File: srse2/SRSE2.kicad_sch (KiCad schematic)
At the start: 83 parts, among them J1 s88-N, J2 CAN, J3 RJ45_Hanrun_HR911105A_Horizon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, P1 I2S, P10 PIC_SPARE, P11 RS485 TERM, P12 RS485, P13 CONN_01X03, P15 RA5, P17 RA5, P18 CONN_01X03, P19 CONN_01X02, P2 CONN_01X09, P20 O2P-Rst, P3 CONN_01X02, P4 CONN_01X04, P5 CONN_01X04, P6 ISO_I2C, P7 CAN_TERM, P8 CAN, P9 PIC_I2C, U1 Omega2, U2 ADuM1250, U3 SN65HVD230, U4 PIC18F25K80, U6 MAX485, U7 TPS5430DDA, U8 CD4504, U9 LM317, Y1 16MHz

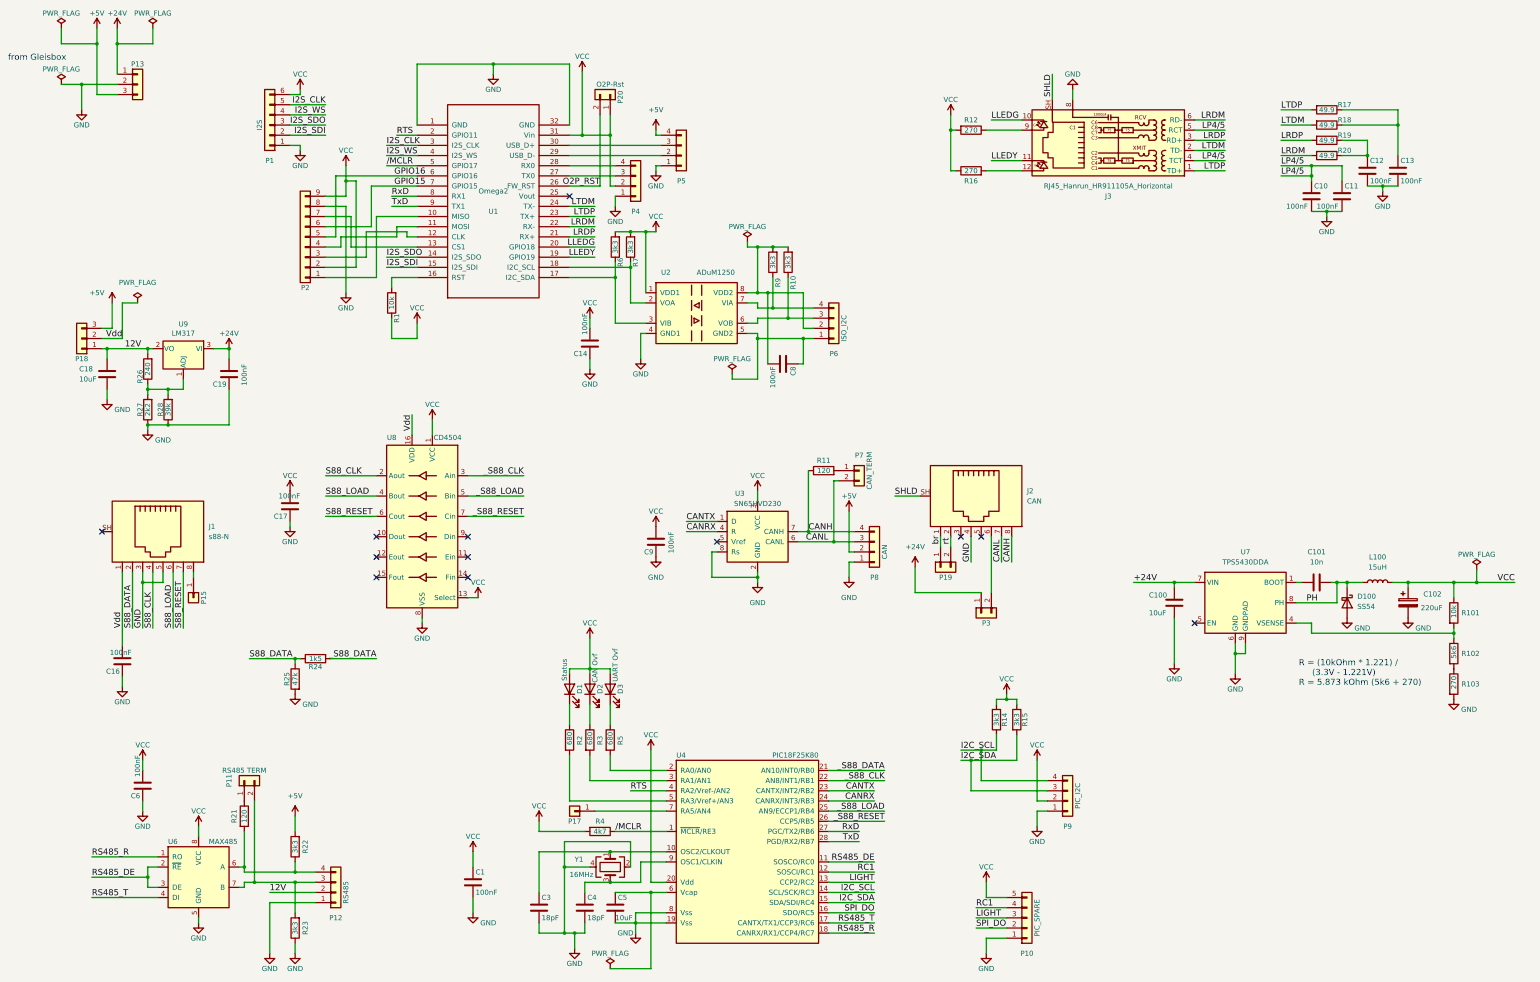
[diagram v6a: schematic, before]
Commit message: update to KiCad 7.0 - wip
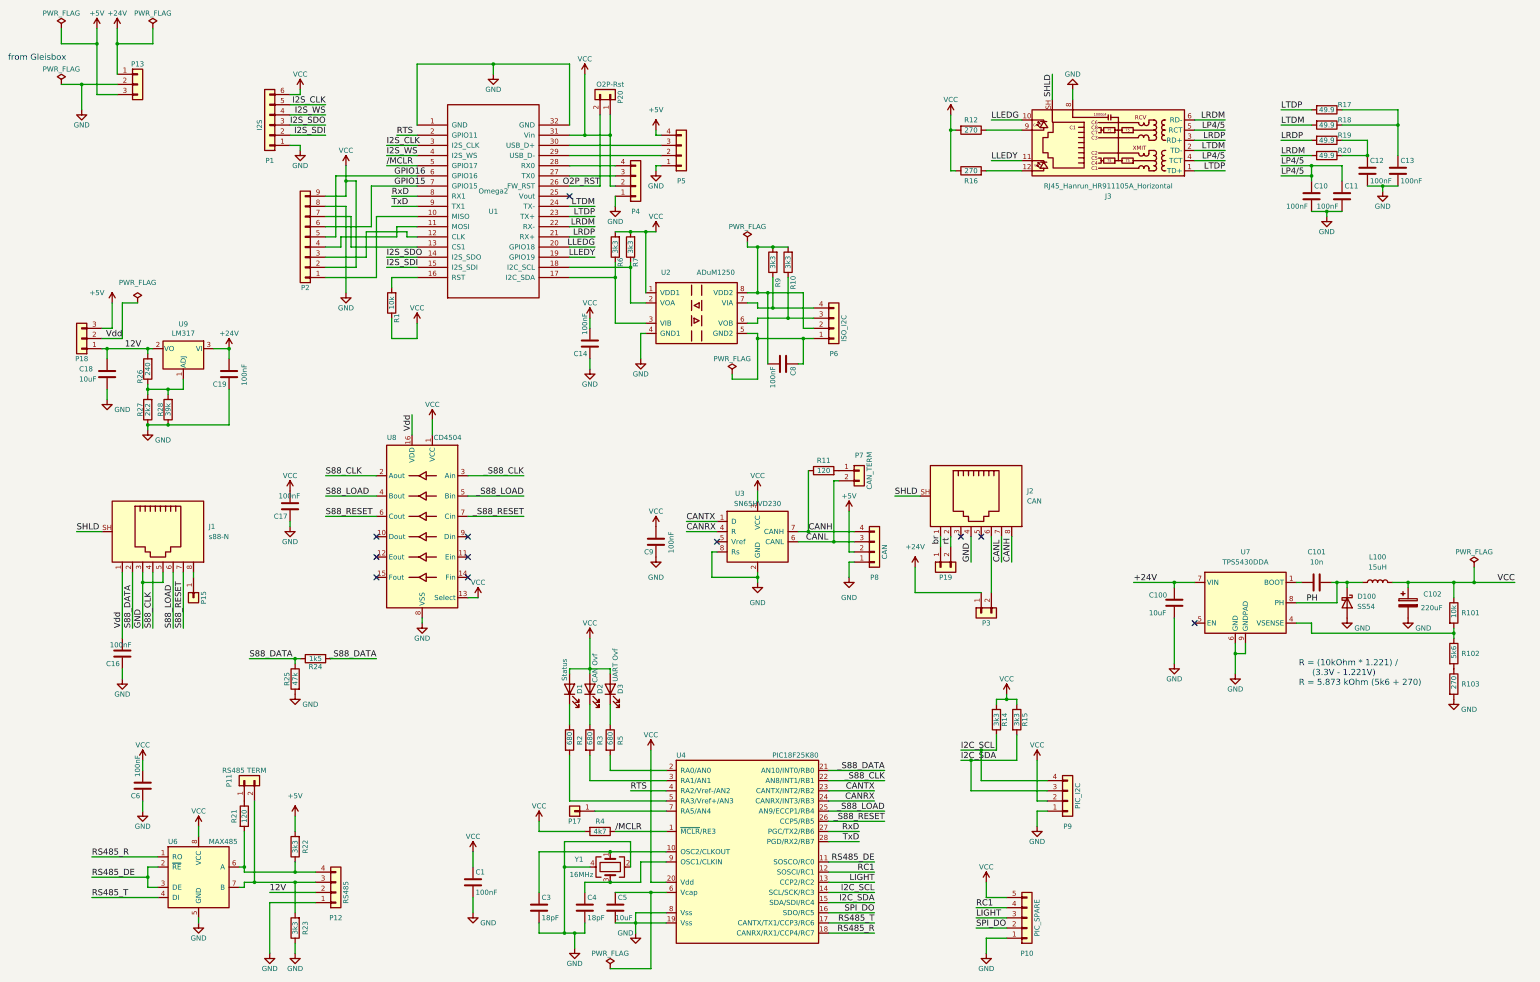
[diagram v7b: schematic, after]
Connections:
- net SHLD: now also J1.SH
- no-connect marks 12 -> 11
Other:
- moved on the sheet: C16
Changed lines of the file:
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@@
   (junction (at 175.26 86.36) (diameter 0) (color 0 0 0 0)
   )
-  (junction (at 386.715 173.99) (diameter 0) (color 0 0 0 0)
-  )
   (junction (at 175.26 95.25) (diameter 0) (color 0 0 0 0)
   )
@@
   (junction (at 354.33 173.99) (diameter 0) (color 0 0 0 0)
   )
+  (junction (at 386.08 173.99) (diameter 0) (color 0 0 0 0)
+  )
   (junction (at 158.75 261.62) (diameter 0) (color 0 0 0 0)
   )
@@
   (junction (at 207.01 113.03) (diameter 0) (color 0 0 0 0)
   )
-  (junction (at 163.195 62.23) (diameter 0) (color 0 0 0 0)
+  (junction (at 163.83 62.23) (diameter 0) (color 0 0 0 0)
   )
   (junction (at 367.03 59.69) (diameter 0) (color 0 0 0 0)
@@
   (no_connect (at 196.85 163.83))
   (no_connect (at 262.89 162.56))
-  (no_connect (at 43.18 161.29))
   (no_connect (at 111.76 167.64))
   (no_connect (at 111.76 162.56))
@@
     (stroke (width 0) (type default))
   )
+  (wire (pts (xy 163.83 62.23) (xy 170.18 62.23))
+    (stroke (width 0) (type default))
+  )
   (wire (pts (xy 74.93 125.73) (xy 74.93 134.62))
     (stroke (width 0) (type default))
@@
     (stroke (width 0) (type default))
   )
-  (wire (pts (xy 386.715 170.815) (xy 386.715 173.99))
+  (wire (pts (xy 386.08 170.18) (xy 386.08 173.99))
     (stroke (width 0) (type default))
   )
@@
     (stroke (width 0) (type default))
   )
-  (wire (pts (xy 386.715 173.99) (xy 396.24 173.99))
-    (stroke (width 0) (type default))
-  )
   (wire (pts (xy 163.83 261.62) (xy 163.83 259.08))
     (stroke (width 0) (type default))
@@
     (stroke (width 0) (type default))
   )
-  (wire (pts (xy 160.02 62.23) (xy 163.195 62.23))
-    (stroke (width 0) (type default))
-  )
   (wire (pts (xy 166.37 231.14) (xy 184.15 231.14))
     (stroke (width 0) (type default))
@@
     (stroke (width 0) (type default))
   )
+  (wire (pts (xy 163.83 46.99) (xy 163.83 62.23))
+    (stroke (width 0) (type default))
+  )
   (wire (pts (xy 204.47 90.17) (xy 204.47 88.9))
     (stroke (width 0) (type default))
@@
     (stroke (width 0) (type default))
   )
+  (wire (pts (xy 48.26 195.58) (xy 48.26 198.12))
+    (stroke (width 0) (type default))
+  )
   (wire (pts (xy 229.87 156.21) (xy 229.87 166.37))
     (stroke (width 0) (type default))
@@
     (stroke (width 0) (type default))
   )
+  (wire (pts (xy 386.08 173.99) (xy 396.24 173.99))
+    (stroke (width 0) (type default))
+  )
   (wire (pts (xy 316.23 58.42) (xy 323.85 58.42))
     (stroke (width 0) (type default))
@@
     (stroke (width 0) (type default))
   )
-  (wire (pts (xy 163.195 62.23) (xy 170.18 62.23))
-    (stroke (width 0) (type default))
-  )
   (wire (pts (xy 359.41 74.93) (xy 363.22 74.93))
     (stroke (width 0) (type default))
@@
     (stroke (width 0) (type default))
   )
+  (wire (pts (xy 36.83 161.29) (xy 43.18 161.29))
+    (stroke (width 0) (type default))
+  )
   (wire (pts (xy 121.92 59.69) (xy 121.92 44.45))
     (stroke (width 0) (type default))
@@
     (stroke (width 0) (type default))
   )
-  (wire (pts (xy 48.26 197.485) (xy 48.26 200.025))
-    (stroke (width 0) (type default))
-  )
   (wire (pts (xy 91.44 264.16) (xy 91.44 266.7))
     (stroke (width 0) (type default))
@@
     (stroke (width 0) (type default))
   )
-  (wire (pts (xy 381 173.99) (xy 386.715 173.99))
+  (wire (pts (xy 381 173.99) (xy 386.08 173.99))
     (stroke (width 0) (type default))
   )
@@
     (stroke (width 0) (type default))
   )
-  (wire (pts (xy 163.195 46.355) (xy 163.195 62.23))
-    (stroke (width 0) (type default))
-  )
   (wire (pts (xy 99.06 147.32) (xy 111.76 147.32))
     (stroke (width 0) (type default))
@@
     (stroke (width 0) (type default))
   )
-  (wire (pts (xy 48.26 171.45) (xy 48.26 189.865))
+  (wire (pts (xy 160.02 62.23) (xy 163.83 62.23))
+    (stroke (width 0) (type default))
+  )
+  (wire (pts (xy 48.26 171.45) (xy 48.26 187.96))
     (stroke (width 0) (type default))
   )
@@
     (effects (font (size 1.524 1.524)) (justify left bottom))
   )
+  (label "SHLD" (at 36.83 161.29 0) (fields_autoplaced)
+    (effects (font (size 1.524 1.524)) (justify left bottom))
+  )
   (label "_S88_LOAD" (at 238.76 231.14 180) (fields_autoplaced)
     (effects (font (size 1.524 1.524)) (justify right bottom))
@@
     )
   )
-  (symbol (lib_id "Device:C") (at 48.26 193.675 180) (unit 1)
+  (symbol (lib_id "Device:C") (at 48.26 191.77 180) (unit 1)
     (in_bom yes) (on_board yes) (dnp no)
-    (property "Reference" "C16" (at 47.625 196.215 0)
+    (property "Reference" "C16" (at 47.625 194.31 0)
       (effects (font (size 1.27 1.27)) (justify left))
     )
-    (property "Value" "100nF" (at 50.546 191.516 0)
+    (property "Value" "100nF" (at 50.546 189.611 0)
       (effects (font (size 1.27 1.27)) (justify left))
     )
-    (property "Footprint" "Capacitor_SMD:C_0805_2012Metric_Pad1.18x1.45mm_HandSolder" (at 47.2948 189.865 0)
+    (property "Footprint" "Capacitor_SMD:C_0805_2012Metric_Pad1.18x1.45mm_HandSolder" (at 47.2948 187.96 0)
       (effects (font (size 1.27 1.27)) hide)
     )
-    (property "Datasheet" "~" (at 48.26 193.675 0)
+    (property "Datasheet" "~" (at 48.26 191.77 0)
       (effects (font (size 1.27 1.27)))
     )
-    (property "LCSC" "C49678" (at 48.26 193.675 0)
+    (property "LCSC" "C49678" (at 48.26 191.77 0)
       (effects (font (size 1.27 1.27)) hide)
     )
@@
     )
   )
-  (symbol (lib_name "GND_1") (lib_id "power:GND") (at 48.26 200.025 0) (unit 1)
+  (symbol (lib_name "GND_1") (lib_id "power:GND") (at 48.26 198.12 0) (unit 1)
     (in_bom yes) (on_board yes) (dnp no)
-    (property "Reference" "#PWR051" (at 48.26 206.375 0)
+    (property "Reference" "#PWR051" (at 48.26 204.47 0)
       (effects (font (size 1.27 1.27)) hide)
     )
-    (property "Value" "GND" (at 48.26 203.835 0)
+    (property "Value" "GND" (at 48.26 201.93 0)
       (effects (font (size 1.27 1.27)))
     )
-    (property "Footprint" "" (at 48.26 200.025 0)
+    (property "Footprint" "" (at 48.26 198.12 0)
       (effects (font (size 1.27 1.27)) hide)
     )
-    (property "Datasheet" "" (at 48.26 200.025 0)
+    (property "Datasheet" "" (at 48.26 198.12 0)
       (effects (font (size 1.27 1.27)) hide)
     )
@@
     )
   )
-  (symbol (lib_name "VCC_1") (lib_id "power:VCC") (at 163.195 46.355 0) (unit 1)
+  (symbol (lib_name "VCC_1") (lib_id "power:VCC") (at 163.83 46.99 0) (unit 1)
     (in_bom yes) (on_board yes) (dnp no)
-    (property "Reference" "#PWR014" (at 163.195 50.165 0)
+    (property "Reference" "#PWR014" (at 163.83 50.8 0)
       (effects (font (size 1.27 1.27)) hide)
     )
-    (property "Value" "VCC" (at 163.195 42.545 0)
+    (property "Value" "VCC" (at 163.83 43.18 0)
       (effects (font (size 1.27 1.27)))
     )
-    (property "Footprint" "" (at 163.195 46.355 0)
+    (property "Footprint" "" (at 163.83 46.99 0)
       (effects (font (size 1.27 1.27)) hide)
     )
-    (property "Datasheet" "" (at 163.195 46.355 0)
+    (property "Datasheet" "" (at 163.83 46.99 0)
       (effects (font (size 1.27 1.27)) hide)
     )
@@
     )
   )
-  (symbol (lib_name "PWR_FLAG_2") (lib_id "power:PWR_FLAG") (at 386.715 170.815 0) (unit 1)
+  (symbol (lib_name "PWR_FLAG_2") (lib_id "power:PWR_FLAG") (at 386.08 170.18 0) (unit 1)
     (in_bom yes) (on_board yes) (dnp no)
-    (property "Reference" "#FLG08" (at 386.715 168.91 0)
+    (property "Reference" "#FLG08" (at 386.08 168.275 0)
       (effects (font (size 1.27 1.27)) hide)
     )
-    (property "Value" "PWR_FLAG" (at 386.715 167.005 0)
+    (property "Value" "PWR_FLAG" (at 386.08 166.37 0)
       (effects (font (size 1.27 1.27)))
     )
-    (property "Footprint" "" (at 386.715 170.815 0)
+    (property "Footprint" "" (at 386.08 170.18 0)
       (effects (font (size 1.27 1.27)) hide)
     )
-    (property "Datasheet" "~" (at 386.715 170.815 0)
+    (property "Datasheet" "~" (at 386.08 170.18 0)
       (effects (font (size 1.27 1.27)) hide)
     )

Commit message: use 18V symbol instead of 24V
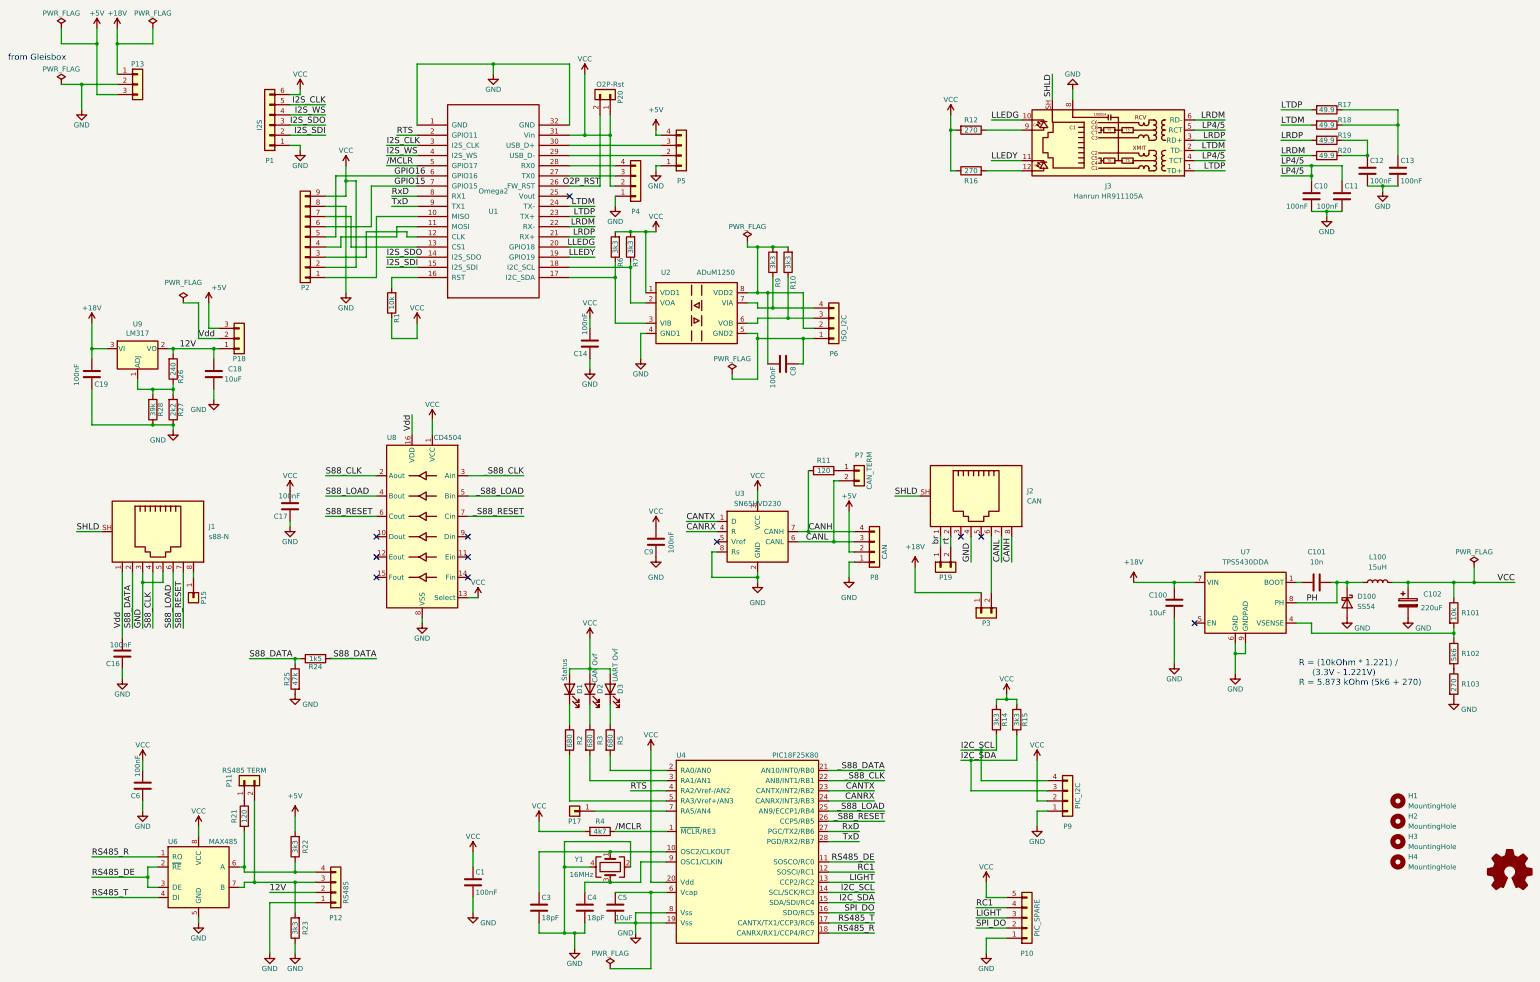
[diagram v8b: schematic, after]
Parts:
- added H1, H2, H3, H4: MountingHole, srse2:MountingHole_3mm, symbol Mechanical:MountingHole
- J3: value RJ45_Hanrun_HR911105A_Horizontal -> Hanrun HR911105A
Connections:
- net +24V renamed +18V
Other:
- moved on the sheet: C18, C19, P18, R26, R27, R28, U9
